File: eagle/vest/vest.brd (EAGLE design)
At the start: 100 x 80 mm, 20 parts, among them IC1 74HCT245

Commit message: wip
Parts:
- added C2, C3, C4, C5: (no value), rcl:C025-025X050
- added C6: 470uF, rcl:TT2D7L
- added JP1: (no value), microbuilder:1X08_ROUND_70
- added PWR+, PWR-: WIREPAD4,16O1,6, wirepad:4,16O1,6
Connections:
- net 3.3V: now also J1.7, J1.8, JP1.7, JP1.8
- net BTN1: now also C5.1, JP1.5, U$1.18/A4
- net BTN2: now also C4.1, JP1.6, U$1.19/A5
- net GND: now also C2.2, C3.2, C4.2, C5.2, C6.-, JP1.2, JP1.4, PWR-.1
- net POT1: now also C2.1, JP1.1, U$1.22/A8
- net POT2: now also C3.1, JP1.3, U$1.23/A9
- net VCC: now also C6.+, PWR+.1; no longer J1.7, J1.8
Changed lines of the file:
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@@
 <element name="C1" library="rcl" package="C025-025X050" value="" x="-38.1" y="-81.28"/>
 <element name="J1" library="con-amp" package="215877-4" value="" x="-30.48" y="-93.98"/>
+<element name="C2" library="rcl" package="C025-025X050" value="" x="-38.1" y="-105.41"/>
+<element name="C3" library="rcl" package="C025-025X050" value="" x="-38.1" y="-110.49"/>
+<element name="C4" library="rcl" package="C025-025X050" value="" x="-38.1" y="-115.57"/>
+<element name="C5" library="rcl" package="C025-025X050" value="" x="-38.1" y="-120.65"/>
+<element name="JP1" library="microbuilder" package="1X08_ROUND_70" value="" x="-30.48" y="-125.73"/>
+<element name="PWR+" library="wirepad" package="4,16O1,6" value="WIREPAD4,16O1,6" x="-38.1" y="-130.81"/>
+<element name="PWR-" library="wirepad" package="4,16O1,6" value="WIREPAD4,16O1,6" x="-38.1" y="-137.16"/>
+<element name="C6" library="rcl" package="TT2D7L" value="470uF" x="-45.72" y="-137.16"/>
 </elements>
 <signals>
@@
 <contactref element="J1" pad="4"/>
 <contactref element="IC1" pad="19"/>
-<wire x1="-33.655" y1="-85.09" x2="-36.83" y2="-81.28" width="0" layer="19" extent="1-1"/>
+<contactref element="C5" pad="2"/>
+<contactref element="C3" pad="2"/>
+<contactref element="C2" pad="2"/>
+<contactref element="C4" pad="2"/>
+<contactref element="JP1" pad="2"/>
+<contactref element="JP1" pad="4"/>
+<contactref element="PWR-" pad="1"/>
+<contactref element="C6" pad="-"/>
+<wire x1="-38.1" y1="-137.16" x2="-44.45" y2="-137.16" width="0" layer="19" extent="1-1"/>
+<wire x1="-36.83" y1="-125.73" x2="-38.1" y2="-137.16" width="0" layer="19" extent="1-1"/>
+<wire x1="-36.83" y1="-120.65" x2="-36.83" y2="-125.73" width="0" layer="19" extent="1-1"/>
+<wire x1="-31.75" y1="-125.73" x2="-36.83" y2="-125.73" width="0" layer="19" extent="1-1"/>
+<wire x1="-36.83" y1="-115.57" x2="-36.83" y2="-120.65" width="0" layer="19" extent="1-1"/>
+<wire x1="-36.83" y1="-110.49" x2="-36.83" y2="-115.57" width="0" layer="19" extent="1-1"/>
+<wire x1="-36.83" y1="-105.41" x2="-36.83" y2="-110.49" width="0" layer="19" extent="1-1"/>
+<wire x1="-33.655" y1="-85.09" x2="-36.83" y2="-105.41" width="0" layer="19" extent="1-1"/>
 <wire x1="-31.115" y1="-85.09" x2="-33.655" y2="-85.09" width="0" layer="19" extent="1-1"/>
+<wire x1="-36.83" y1="-81.28" x2="-33.655" y2="-85.09" width="0" layer="19" extent="1-1"/>
 <wire x1="-39.37" y1="-74.93" x2="-36.83" y2="-81.28" width="0" layer="19" extent="1-1"/>
 <wire x1="-39.37" y1="-69.85" x2="-39.37" y2="-74.93" width="0" layer="19" extent="1-1"/>
@@
 </signal>
 <signal name="3.3V">
+<contactref element="J1" pad="7"/>
+<contactref element="JP1" pad="7"/>
+<contactref element="J1" pad="8"/>
+<contactref element="JP1" pad="8"/>
+<contactref element="U$1" pad="3.3V1"/>
 <contactref element="U$1" pad="3.3V"/>
-<contactref element="U$1" pad="3.3V1"/>
+<wire x1="-21.59" y1="-125.73" x2="-24.13" y2="-125.73" width="0" layer="19" extent="1-1"/>
+<wire x1="-27.305" y1="-87.63" x2="-24.13" y2="-125.73" width="0" layer="19" extent="1-1"/>
+<wire x1="-26.035" y1="-85.09" x2="-27.305" y2="-87.63" width="0" layer="19" extent="1-1"/>
+<wire x1="-30.48" y1="2.54" x2="-26.035" y2="-85.09" width="0" layer="19" extent="1-1"/>
 <wire x1="-20.32" y1="30.48" x2="-30.48" y2="2.54" width="0" layer="19" extent="1-1"/>
 </signal>
@@
 <contactref element="C1" pad="1"/>
 <contactref element="U$1" pad="VIN"/>
-<contactref element="J1" pad="7"/>
-<contactref element="J1" pad="8"/>
 <contactref element="IC1" pad="1"/>
+<contactref element="PWR+" pad="1"/>
+<contactref element="C6" pad="+"/>
+<wire x1="-38.1" y1="-130.81" x2="-46.99" y2="-137.16" width="0" layer="19" extent="1-1"/>
+<wire x1="-39.37" y1="-81.28" x2="-38.1" y2="-130.81" width="0" layer="19" extent="1-1"/>
 <wire x1="-34.29" y1="-74.93" x2="-39.37" y2="-81.28" width="0" layer="19" extent="1-1"/>
 <wire x1="-34.29" y1="-69.85" x2="-34.29" y2="-74.93" width="0" layer="19" extent="1-1"/>
@@
 <wire x1="-34.29" y1="-49.53" x2="-34.29" y2="-54.61" width="0" layer="19" extent="1-1"/>
 <wire x1="-34.29" y1="-44.45" x2="-34.29" y2="-49.53" width="0" layer="19" extent="1-1"/>
-<wire x1="-26.035" y1="-85.09" x2="-34.29" y2="-74.93" width="0" layer="19" extent="1-1"/>
-<wire x1="-27.305" y1="-87.63" x2="-26.035" y2="-85.09" width="0" layer="19" extent="1-1"/>
 <wire x1="-20.32" y1="35.56" x2="-34.29" y2="-44.45" width="0" layer="19" extent="1-1"/>
 <wire x1="-13.97" y1="52.07" x2="-20.32" y2="35.56" width="0" layer="19" extent="1-1"/>
@@
 <signal name="POT1">
 <contactref element="J1" pad="1"/>
+<contactref element="C2" pad="1"/>
+<contactref element="JP1" pad="1"/>
+<contactref element="U$1" pad="22/A8"/>
+<wire x1="-39.37" y1="-105.41" x2="-39.37" y2="-125.73" width="0" layer="19" extent="1-1"/>
+<wire x1="-34.925" y1="-87.63" x2="-39.37" y2="-105.41" width="0" layer="19" extent="1-1"/>
+<wire x1="-20.32" y1="25.4" x2="-34.925" y2="-87.63" width="0" layer="19" extent="1-1"/>
 </signal>
 <signal name="POT2">
 <contactref element="J1" pad="3"/>
+<contactref element="C3" pad="1"/>
+<contactref element="JP1" pad="3"/>
+<contactref element="U$1" pad="23/A9"/>
+<wire x1="-39.37" y1="-110.49" x2="-34.29" y2="-125.73" width="0" layer="19" extent="1-1"/>
+<wire x1="-32.385" y1="-87.63" x2="-39.37" y2="-110.49" width="0" layer="19" extent="1-1"/>
+<wire x1="-20.32" y1="27.94" x2="-32.385" y2="-87.63" width="0" layer="19" extent="1-1"/>
 </signal>
 <signal name="BTN1">
 <contactref element="J1" pad="5"/>
+<contactref element="C5" pad="1"/>
+<contactref element="JP1" pad="5"/>
+<contactref element="U$1" pad="18/A4"/>
+<wire x1="-29.21" y1="-125.73" x2="-39.37" y2="-120.65" width="0" layer="19" extent="1-1"/>
+<wire x1="-29.845" y1="-87.63" x2="-39.37" y2="-120.65" width="0" layer="19" extent="1-1"/>
+<wire x1="-20.32" y1="15.24" x2="-29.845" y2="-87.63" width="0" layer="19" extent="1-1"/>
 </signal>
 <signal name="BTN2">
 <contactref element="J1" pad="6"/>
+<contactref element="C4" pad="1"/>
+<contactref element="JP1" pad="6"/>
+<contactref element="U$1" pad="19/A5"/>
+<wire x1="-26.67" y1="-125.73" x2="-39.37" y2="-115.57" width="0" layer="19" extent="1-1"/>
+<wire x1="-28.575" y1="-85.09" x2="-39.37" y2="-115.57" width="0" layer="19" extent="1-1"/>
+<wire x1="-20.32" y1="17.78" x2="-28.575" y2="-85.09" width="0" layer="19" extent="1-1"/>
 </signal>
 </signals>

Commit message: vest before autorouter
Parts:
- added AUX1, AUX2: (no value), microbuilder:1X03_OVAL
- added H1, H2, H3, H4: MOUNT-HOLE3.0, holes:3,0
- R1, R2, R3, R4, R5, R6, R7, R8: device rcl:0207/10 -> rcl:0204/7
- moved C3 188.5 mm to (79.8, 36.6), turned to 270 degrees
- moved JP1 184.9 mm to (67.6, 31.0), turned to 180 degrees
- moved C5 184.7 mm to (57.1, 37.6), turned to 180 degrees
- moved C2 182.8 mm to (77.0, 36.6), turned to 90 degrees
- moved C4 178.0 mm to (57.1, 34.8), turned to 180 degrees
- moved J1 168.4 mm to (67.6, 42.9), turned to 180 degrees
- moved C6 166.0 mm to (3.56, 21.3)
- moved C1 156.3 mm to (74.9, 26.7), turned to 90 degrees
- moved PWR+ 152.8 mm to (2.54, 16.5)
- moved PWR- 152.8 mm to (2.54, 10.2)
- moved LED2 113.6 mm to (66.0, 3.81)
- moved R1 110.1 mm to (74.9, 10.2), turned to 270 degrees
- moved LED3 108.1 mm to (57.1, 3.81)
- moved LED1 103.4 mm to (74.9, 3.81)
- moved LED4 103.2 mm to (48.3, 3.81)
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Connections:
- new net AUX1: AUX1.2, U$1.12
- new net AUX2: AUX2.2, U$1.17/A3
- net GND: now also AUX1.1, AUX2.1
- net VCC: now also AUX1.3, AUX2.3
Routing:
- net N$2: track 0.00 -> 36.9 mm
- net N$9: track 0.00 -> 31.0 mm
- net N$8: track 0.00 -> 25.1 mm
- net N$7: track 0.00 -> 18.9 mm
- net POT2: track 0.00 -> 13.4 mm
- net N$3: track 0.00 -> 12.8 mm
- net N$6: track 0.00 -> 12.7 mm
- net N$4: track 0.00 -> 6.40 mm
- net N$5: track 0.00 -> 5.88 mm
- net POT1: track 0.00 -> 5.48 mm
- net N$1: track 0.00 -> 2.54 mm
- net N$17: track 0.00 -> 2.54 mm
- net N$16: track 0.00 -> 2.54 mm
- net N$15: track 0.00 -> 2.54 mm
- net N$14: track 0.00 -> 2.54 mm
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- added copper zone on layer 16, net GND
- added copper zone on layer 1, net VCC
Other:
- board size 100 x 80 mm -> 86.4 x 45 mm

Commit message: vest pcb v1
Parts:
- moved C3 10.5 mm to (73.2, 28.4), turned to 0 degrees
- moved C5 4.50 mm to (58.4, 41.9), turned to 90 degrees
- moved C1 4.44 mm to (73.2, 22.6)
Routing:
- net 3.3V: track 0.00 -> 69.3 mm
- net BTN1: track 0.00 -> 65.4 mm, vias 0 -> 1
- net D14: track 0.00 -> 59.7 mm
- net POT1: track 5.48 -> 60.0 mm
- net BTN2: track 0.00 -> 51.6 mm, vias 0 -> 1
- net D8: track 0.00 -> 46.3 mm, vias 0 -> 1
- net D7: track 0.00 -> 45.7 mm
- net POT2: track 13.4 -> 53.2 mm
- net D2: track 0.00 -> 36.8 mm
- net D6: track 0.00 -> 36.3 mm, vias 0 -> 1
- net D20: track 0.00 -> 33.7 mm, vias 0 -> 2
- net D21: track 0.00 -> 27.8 mm, vias 0 -> 1
- net D5: track 0.00 -> 26.6 mm
- net AUX2: track 0.00 -> 23.3 mm
- net AUX1: track 0.00 -> 7.91 mm
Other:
- board text added: "Eran Rundstein"
- board text added: "Vest PCB, Burning man 2014"

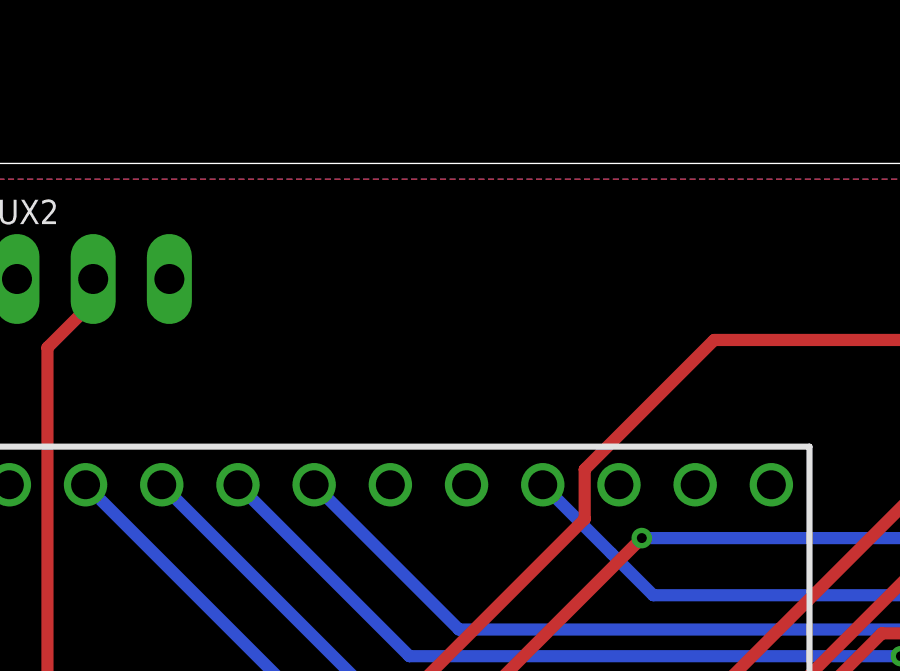
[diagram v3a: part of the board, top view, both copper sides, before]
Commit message: jacket teensy code 'ported' from pants - works but timing sux
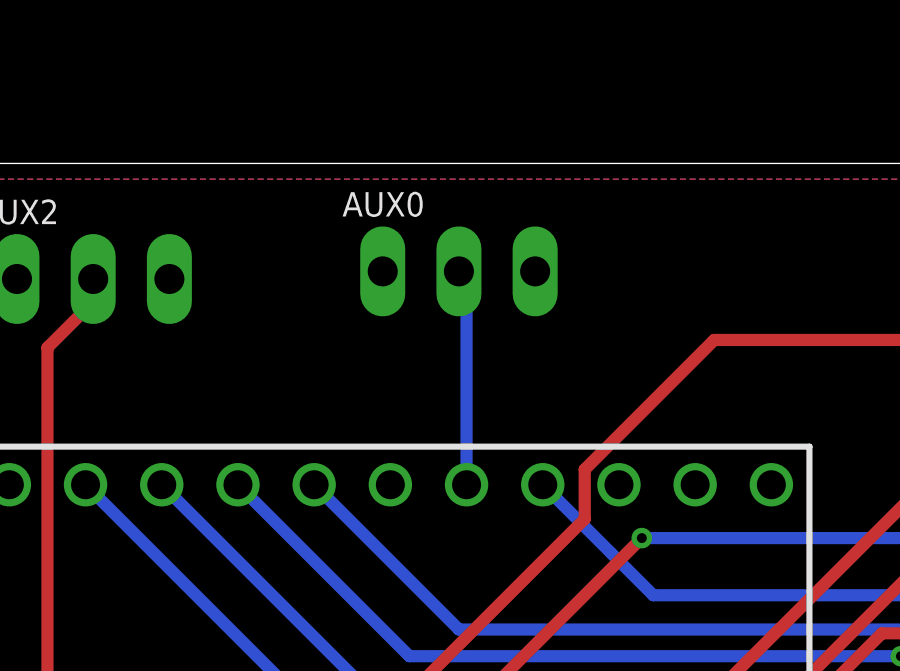
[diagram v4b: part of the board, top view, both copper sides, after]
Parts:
- added AUX0: (no value), microbuilder:1X03_OVAL
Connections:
- new net AUX0: AUX0.2, U$1.3
- net GND: now also AUX0.1
- net VCC: now also AUX0.3
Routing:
- net AUX0: track 0.00 -> 7.22 mm
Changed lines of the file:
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@@
 <element name="H3" library="holes" package="3,0" value="MOUNT-HOLE3.0" x="2.54" y="42.46"/>
 <element name="H4" library="holes" package="3,0" value="MOUNT-HOLE3.0" x="83.82" y="2.54"/>
+<element name="AUX0" library="microbuilder" package="1X03_OVAL" value="" x="31.496" y="41.402"/>
 </elements>
 <signals>
@@
 <vertex x="0.254" y="44.4754"/>
 </polygon>
+<contactref element="AUX0" pad="1"/>
 </signal>
 <signal name="AGND">
@@
 <vertex x="0.254" y="44.4754"/>
 </polygon>
+<contactref element="AUX0" pad="3"/>
 </signal>
 <signal name="N$10">
@@
 <wire x1="19.304" y1="41.148" x2="19.304" y2="40.386" width="0.4064" layer="1"/>
 </signal>
+<signal name="AUX0">
+<contactref element="AUX0" pad="2"/>
+<contactref element="U$1" pad="3"/>
+<wire x1="31.496" y1="41.402" x2="31.75" y2="41.148" width="0.4064" layer="16"/>
+<wire x1="31.75" y1="41.148" x2="31.75" y2="34.29" width="0.4064" layer="16"/>
+</signal>
 </signals>
